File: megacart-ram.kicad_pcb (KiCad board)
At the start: 2 copper layers, 14 parts, among them J1 Conn_02x08_Counter_Clockwise, U1 AS6C4008-55PCN, U10 7432, U11 7432, U12 74LS138, U2 74HC273, U3 74HC74, U4 7421, U5 7421, U6 7402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

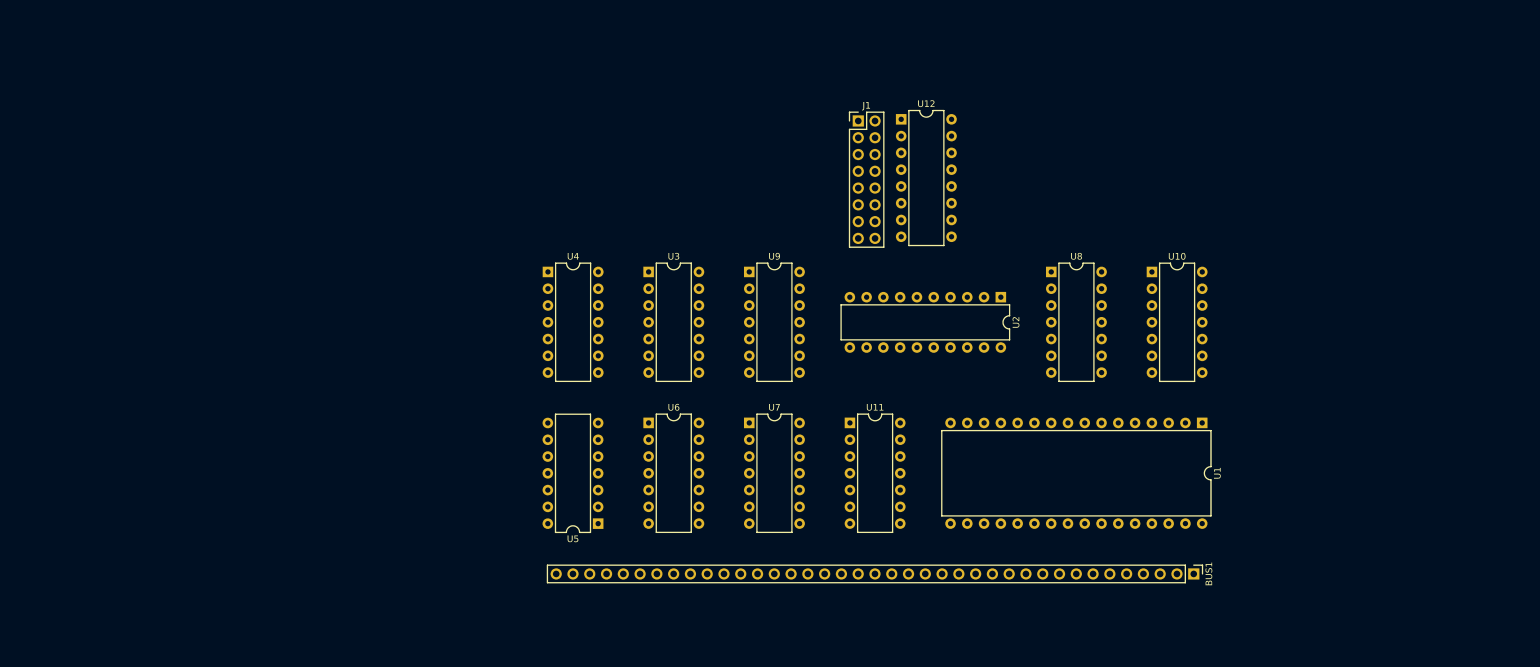
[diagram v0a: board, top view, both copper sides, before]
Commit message: Add decoupling caps and update PCB with RC2014 template.
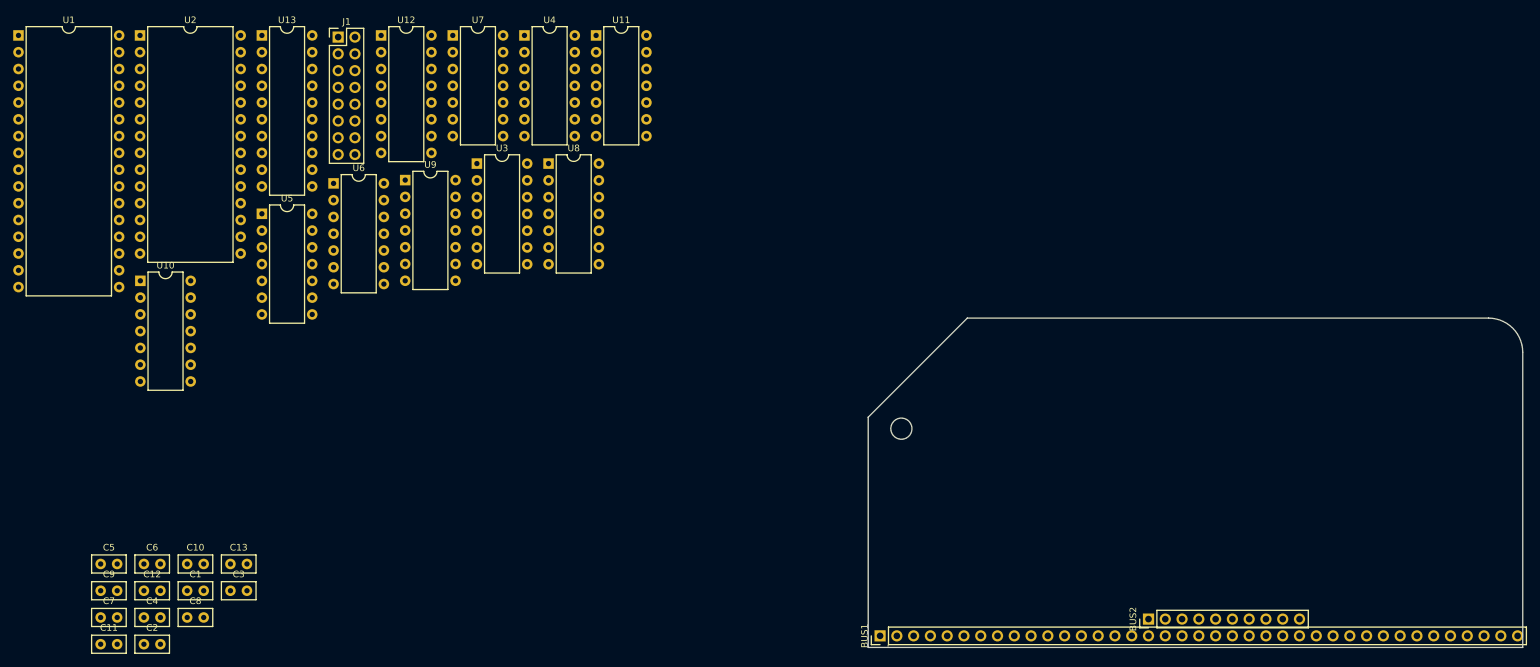
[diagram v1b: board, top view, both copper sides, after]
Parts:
- added ?: , Mounting_Holes:MountingHole_3.2mm_M3, F.Cu at (158.9, 120.2)
- added BUS2: Conn_01x10, Connector_PinHeader_2.54mm:PinHeader_1x10_P2.54mm_Vertical, F.Cu at (196.3, 149.1)
- added C1: C, Capacitor_THT:C_Disc_D5.0mm_W2.5mm_P2.50mm, F.Cu at (50.8, 144.8)
- added C10: C, Capacitor_THT:C_Disc_D5.0mm_W2.5mm_P2.50mm, F.Cu at (50.8, 140.7)
- added C11: C, Capacitor_THT:C_Disc_D5.0mm_W2.5mm_P2.50mm, F.Cu at (37.7, 152.9)
- added C12: C, Capacitor_THT:C_Disc_D5.0mm_W2.5mm_P2.50mm, F.Cu at (44.2, 144.8)
- added C13: C, Capacitor_THT:C_Disc_D5.0mm_W2.5mm_P2.50mm, F.Cu at (57.4, 140.7)
- added C2: C, Capacitor_THT:C_Disc_D5.0mm_W2.5mm_P2.50mm, F.Cu at (44.2, 152.9)
- added C3: C, Capacitor_THT:C_Disc_D5.0mm_W2.5mm_P2.50mm, F.Cu at (57.4, 144.8)
- added C4: C, Capacitor_THT:C_Disc_D5.0mm_W2.5mm_P2.50mm, F.Cu at (44.2, 148.8)
- added C5: C, Capacitor_THT:C_Disc_D5.0mm_W2.5mm_P2.50mm, F.Cu at (37.7, 140.7)
- added C6: C, Capacitor_THT:C_Disc_D5.0mm_W2.5mm_P2.50mm, F.Cu at (44.2, 140.7)
- added C7: C, Capacitor_THT:C_Disc_D5.0mm_W2.5mm_P2.50mm, F.Cu at (37.7, 148.8)
- added C8: C, Capacitor_THT:C_Disc_D5.0mm_W2.5mm_P2.50mm, F.Cu at (50.8, 148.8)
- added C9: C, Capacitor_THT:C_Disc_D5.0mm_W2.5mm_P2.50mm, F.Cu at (37.7, 144.8)
- added U13: 74HC273, Package_DIP:DIP-20_W7.62mm, F.Cu at (62.1, 60.7)
- U2: value 74HC273 -> HM62256BLP; footprint Package_DIP:DIP-20_W7.62mm -> Package_DIP:DIP-28_W15.24mm
- moved U1 188.6 mm to (25.3, 60.7), turned to 0 degrees
- moved U10 153.2 mm to (43.7, 97.9)
- moved U2 136.2 mm to (43.7, 60.7), turned to 0 degrees
- moved J1 79.8 mm to (73.7, 61.0)
- moved U12 79.8 mm to (80.2, 60.7)
- moved U8 77.9 mm to (105.5, 80.1)
- moved U7 73.9 mm to (91.0, 60.7)
- moved U11 70.1 mm to (112.7, 60.7)
- moved U5 69.2 mm to (62.1, 87.7), turned to 0 degrees
- moved U6 59.9 mm to (73.0, 83.1)
- moved U9 53.9 mm to (83.8, 82.6)
- moved BUS1 48.4 mm to (155.7, 151.6), turned to 90 degrees
- moved U4 36.0 mm to (101.9, 60.7)
- moved U3 30.7 mm to (94.7, 80.1)
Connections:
- U10 pad 1: Net-(U6-Pad11) -> Net-(U10-Pad1)
- U10 pad 10: Net-(U8-Pad8) -> Net-(U10-Pad10)
- U10 pad 12: Net-(U6-Pad11) -> Net-(U10-Pad12)
- U10 pad 13: Net-(U8-Pad11) -> Net-(U10-Pad10)
- U10 pad 14: Vcc -> (no net)
- U10 pad 2: Net-(U8-Pad3) -> Net-(U10-Pad10)
- U10 pad 4: Net-(U6-Pad11) -> Net-(U10-Pad4)
- U10 pad 5: Net-(U8-Pad6) -> Net-(U10-Pad10)
- U10 pad 7: Gnd -> (no net)
- U10 pad 9: Net-(U6-Pad11) -> Net-(U10-Pad9)
- U11 pad 1: Net-(U6-Pad11) -> Net-(U11-Pad1)
- U11 pad 10: (no net) -> Net-(U11-Pad10)
- U11 pad 14: Vcc -> (no net)
- U11 pad 2: Net-(U9-Pad3) -> Net-(U10-Pad10)
- U11 pad 6: unconnected-(U11-Pad6) -> ~{MWR}
- U11 pad 7: Gnd -> (no net)
- U11 pad 8: (no net) -> Net-(U11-Pad8)
- U11 pad 9: (no net) -> A15
- U2 pad 1: ~{RESET} -> A14
- U2 pad 10: GND -> A0
- U2 pad 11: Net-(U2-Pad11) -> D0
- U2 pad 12: Net-(U2-Pad12) -> D1
- U2 pad 13: A4 -> D2
- U2 pad 14: unconnected-(U2-Pad14) -> GND
- U2 pad 15: unconnected-(U2-Pad15) -> D3
- U2 pad 16: unconnected-(U2-Pad16) -> D4
- U2 pad 17: unconnected-(U2-Pad17) -> D5
- U2 pad 18: unconnected-(U2-Pad18) -> D6
- U2 pad 19: unconnected-(U2-Pad19) -> D7
- U2 pad 2: Net-(U2-Pad2) -> A12
- U2 pad 20: VCC -> Net-(U11-Pad8)
- U2 pad 3: A0 -> A7
- U2 pad 4: A1 -> A6
- U2 pad 5: Net-(U2-Pad5) -> A5
- U2 pad 6: Net-(U2-Pad6) -> A4
- U2 pad 7: A2 -> A3
- U2 pad 8: A3 -> A2
- U2 pad 9: Net-(U2-Pad9) -> A1
- U3 pad 10: unconnected-(U3-Pad10) -> VCC
- U3 pad 4: unconnected-(U3-Pad4) -> VCC
- U4 pad 14: Vcc -> (no net)
- U4 pad 7: Gnd -> (no net)
- U5 pad 14: Vcc -> (no net)
- U5 pad 7: Gnd -> (no net)
- U5 pad 8: Net-(U2-Pad11) -> Net-(U13-Pad11)
- U6 pad 11: Net-(U6-Pad11) -> Net-(U10-Pad10)
- U6 pad 4: Net-(U6-Pad11) -> Net-(U10-Pad10)
- U7 pad 12: (no net) -> Net-(U11-Pad10)
- U7 pad 13: (no net) -> PAGE
- U8 pad 1: Net-(U7-Pad8) -> Net-(U13-Pad2)
- U8 pad 10: Net-(U2-Pad6) -> Net-(U7-Pad8)
- U8 pad 11: Net-(U8-Pad11) -> Net-(U10-Pad12)
- U8 pad 12: Net-(U7-Pad8) -> Net-(U13-Pad9)
- U8 pad 13: Net-(U2-Pad9) -> Net-(U7-Pad8)
- U8 pad 14: Vcc -> (no net)
- U8 pad 2: Net-(U2-Pad2) -> Net-(U7-Pad8)
- U8 pad 3: Net-(U8-Pad3) -> Net-(U10-Pad1)
- U8 pad 4: Net-(U7-Pad8) -> Net-(U13-Pad5)
- U8 pad 5: Net-(U2-Pad5) -> Net-(U7-Pad8)
- U8 pad 6: Net-(U8-Pad6) -> Net-(U10-Pad4)
- U8 pad 7: Gnd -> (no net)
- U8 pad 8: Net-(U8-Pad8) -> Net-(U10-Pad9)
- U8 pad 9: Net-(U7-Pad8) -> Net-(U13-Pad6)
- U9 pad 1: Net-(U7-Pad8) -> Net-(U13-Pad12)
- U9 pad 14: Vcc -> (no net)
- U9 pad 2: Net-(U2-Pad12) -> Net-(U7-Pad8)
- U9 pad 3: Net-(U9-Pad3) -> Net-(U11-Pad1)
- U9 pad 7: Gnd -> (no net)
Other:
- board outline added: 99.1 x 49.9 mm
- rule pad_to_mask_clearance: 0 -> 0.2

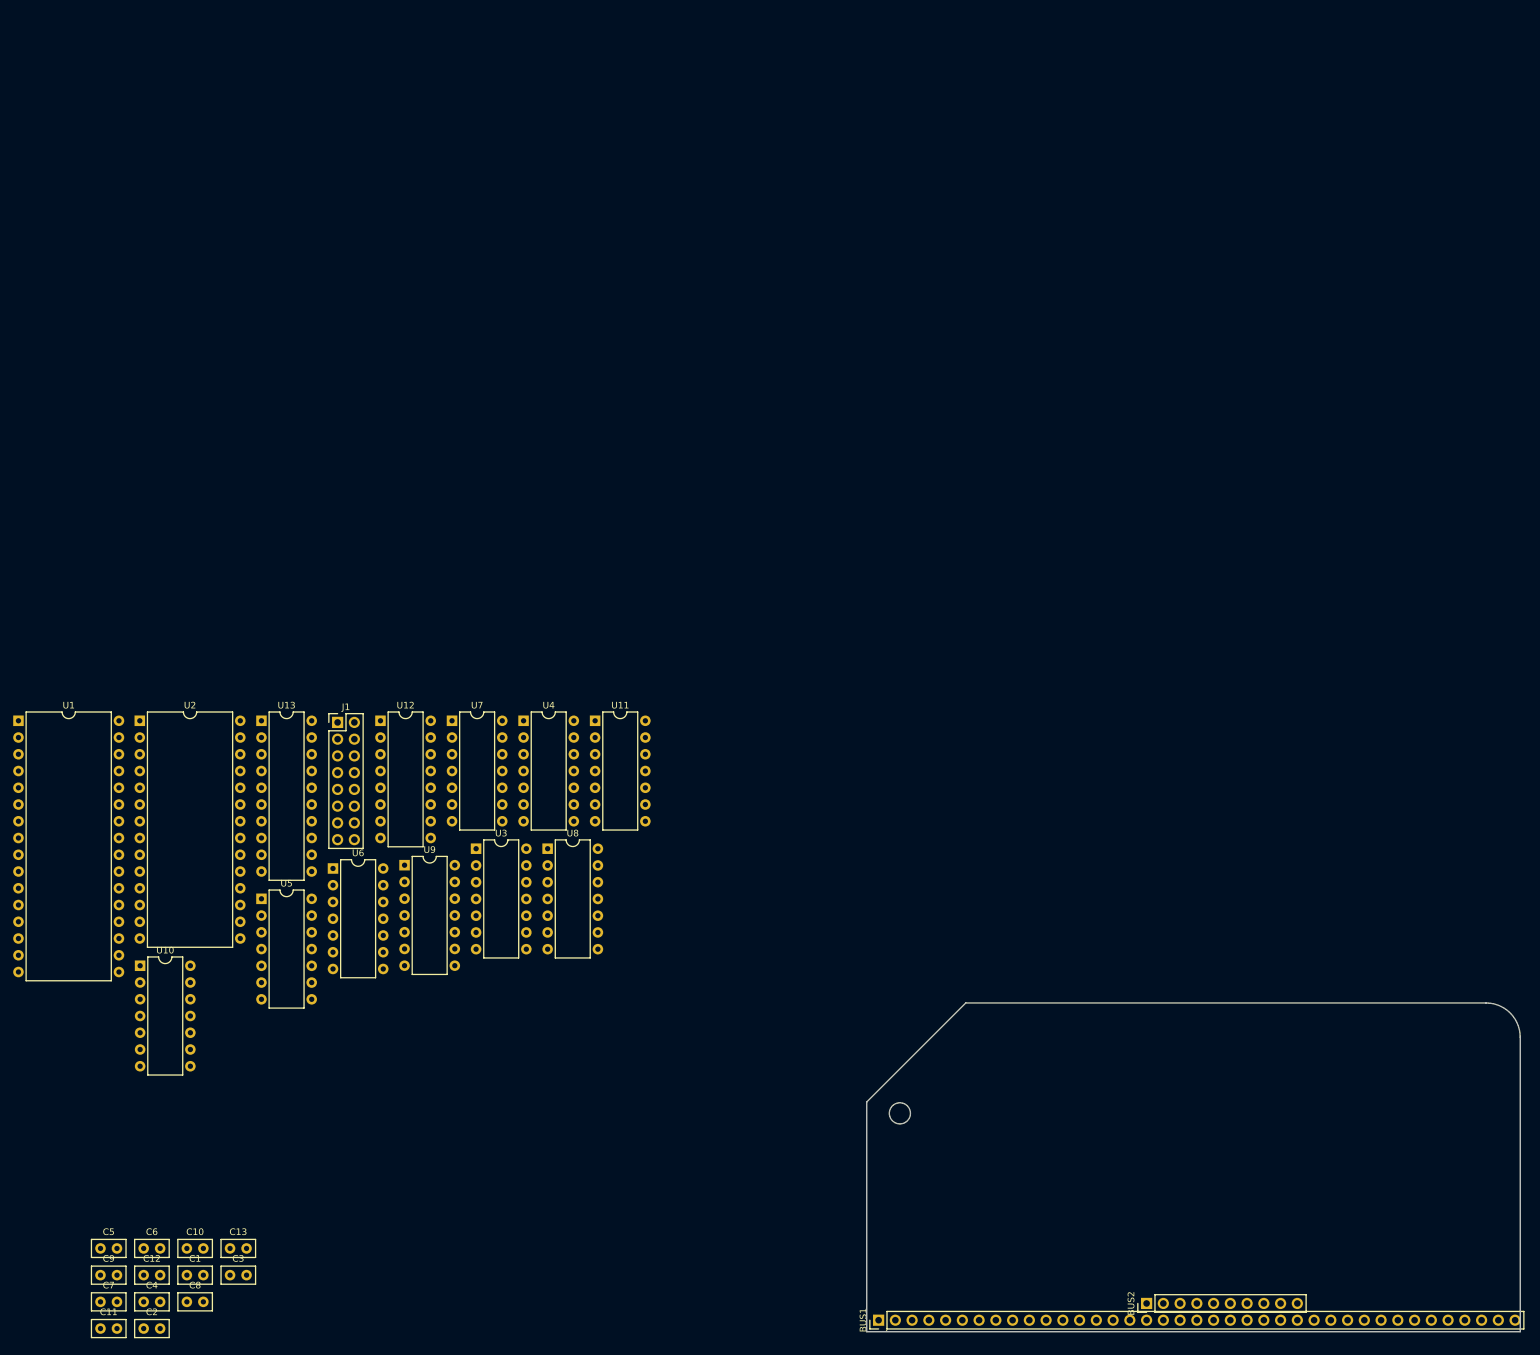
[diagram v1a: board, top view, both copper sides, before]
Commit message: Add explicit power units for 7400 ICs.
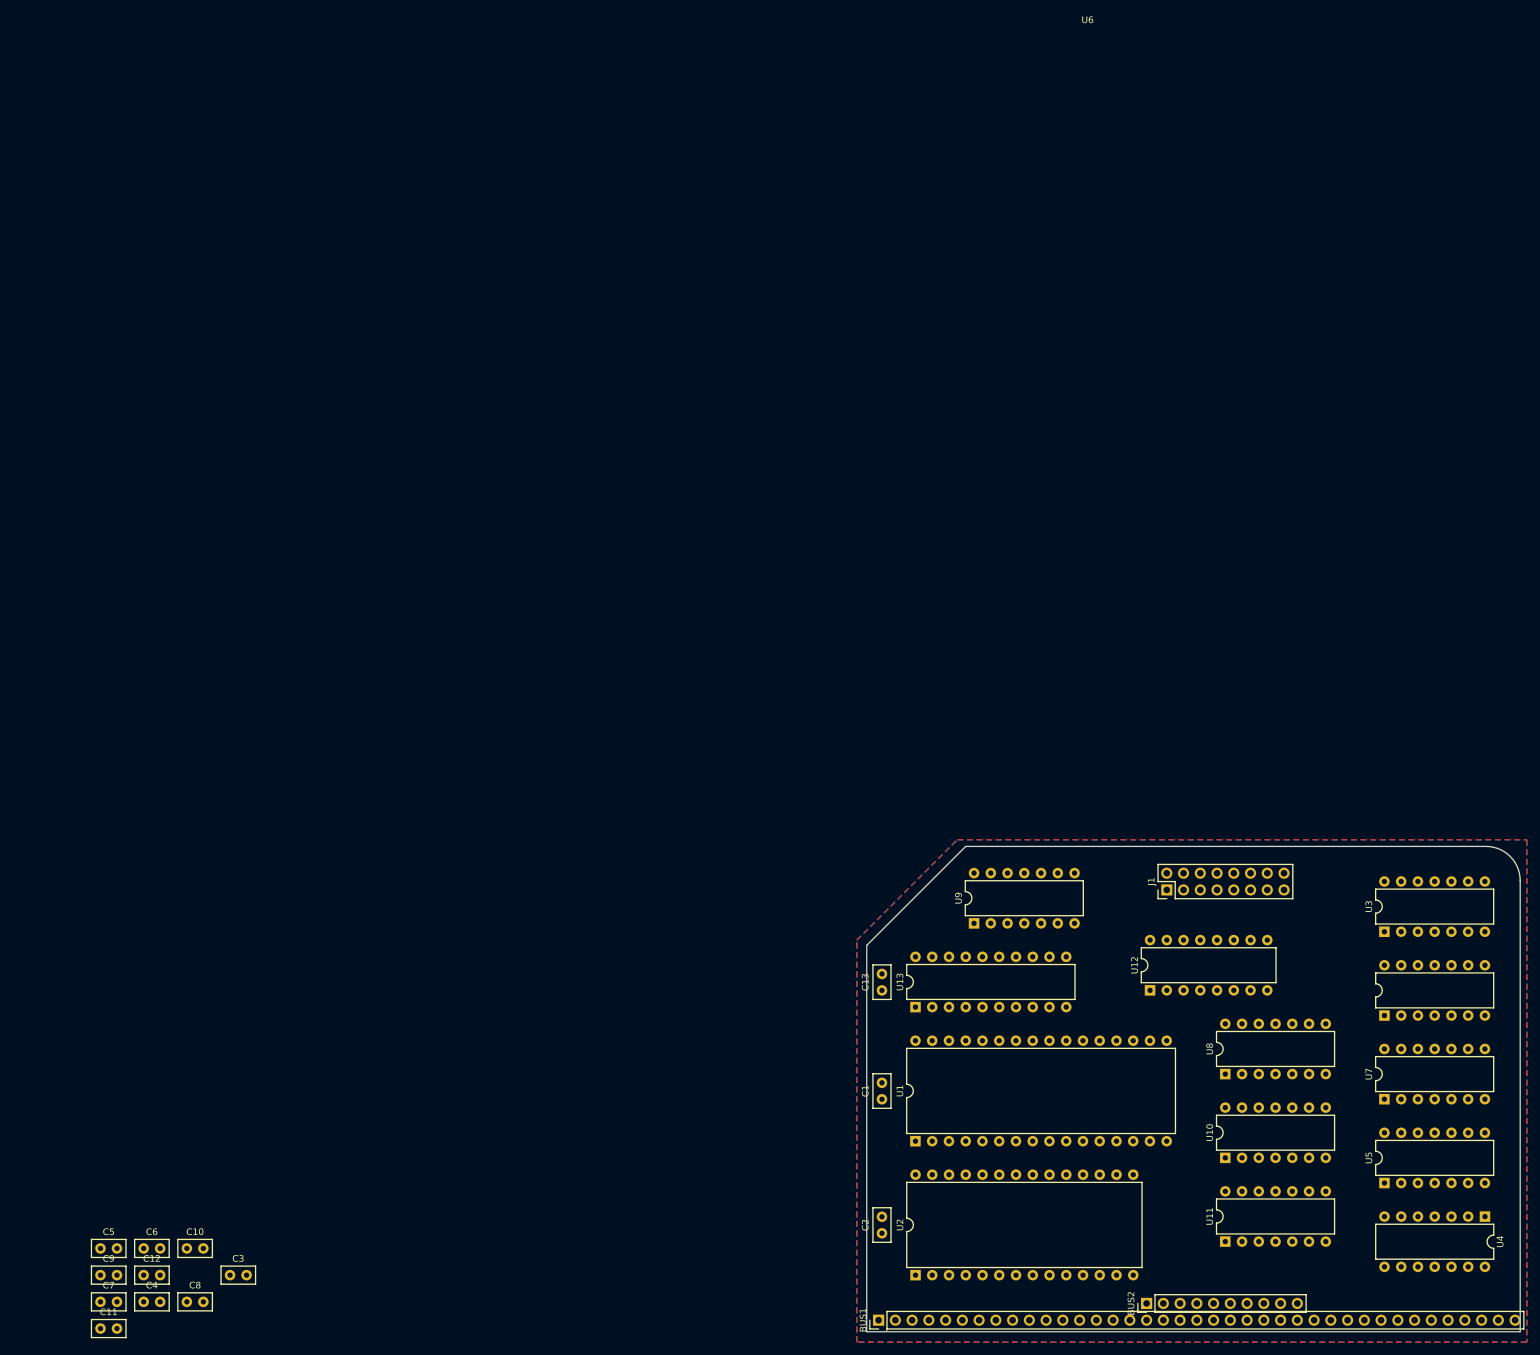
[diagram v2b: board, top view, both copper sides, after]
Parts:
- removed ?: , Mounting_Holes:MountingHole_3.2mm_M3
- moved U5 175.7 mm to (232.4, 130.8), turned to 90 degrees
- moved U10 167.1 mm to (208.3, 127.0), turned to 90 degrees
- moved U4 164.0 mm to (247.7, 135.9), turned to -90 degrees
- moved U6 161.0 mm to (232.4, 105.4), turned to 90 degrees
- moved U7 152.6 mm to (232.4, 118.1), turned to 90 degrees
- moved U1 150.2 mm to (161.3, 124.5), turned to 90 degrees
- moved U2 144.6 mm to (161.3, 144.8), turned to 90 degrees
- moved U3 138.3 mm to (232.4, 92.7), turned to 90 degrees
- moved J1 128.3 mm to (199.4, 86.4), turned to 90 degrees
- moved U11 124.0 mm to (208.3, 139.7), turned to 90 degrees
- moved U12 123.7 mm to (196.9, 101.6), turned to 90 degrees
- moved C2 112.9 mm to (156.2, 138.4), turned to 90 degrees
- moved C1 108.7 mm to (156.2, 118.1), turned to 90 degrees
- moved U8 108.3 mm to (208.3, 114.3), turned to 90 degrees
- moved U13 108.3 mm to (161.3, 104.1), turned to 90 degrees
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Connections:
- U10 pad 14: (no net) -> VCC
- U10 pad 7: (no net) -> GND
- U11 pad 14: (no net) -> VCC
- U11 pad 7: (no net) -> GND
- U4 pad 14: (no net) -> VCC
- U4 pad 7: (no net) -> GND
- U5 pad 14: (no net) -> VCC
- U5 pad 7: (no net) -> GND
- U6 pad 14: (no net) -> VCC
- U6 pad 7: (no net) -> GND
- U7 pad 14: (no net) -> VCC
- U7 pad 7: (no net) -> GND
- U8 pad 14: (no net) -> VCC
- U8 pad 7: (no net) -> GND
- U9 pad 14: (no net) -> VCC
- U9 pad 7: (no net) -> GND
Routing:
- added copper zone on F.Cu, net GND
- added copper zone on B.Cu, net VCC
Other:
- board size 99.1 x 49.9 mm -> 99.1 x 73.6 mm

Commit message: First pass at routing PCB.
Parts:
- removed C4, C5, C8: C, Capacitor_THT:C_Disc_D5.0mm_W2.5mm_P2.50mm
- moved C7 214.1 mm to (250.2, 122.4), turned to 180 degrees
- moved C11 204.8 mm to (230.1, 82.8), turned to -90 degrees
- moved C6 198.9 mm to (238.0, 95.8), turned to -90 degrees
- moved C12 186.9 mm to (231.1, 141.8), turned to -90 degrees
- moved C9 184.1 mm to (220.5, 122.4), turned to 180 degrees
- moved C3 175.7 mm to (231.7, 122.4)
- moved C10 122.8 mm to (163.8, 92.7), turned to 180 degrees
- moved U4 84.3 mm to (182.0, 83.0), turned to 0 degrees
- moved J1 64.4 mm to (247.6, 129.0), turned to 0 degrees
- moved C13 60.3 mm to (207.8, 132.8), turned to 0 degrees
- moved U10 58.3 mm to (170.0, 83.0), turned to 0 degrees
- moved U11 57.5 mm to (218.0, 83.0), turned to 0 degrees
- moved U5 54.6 mm to (206.0, 83.0), turned to 0 degrees
- moved U9 49.2 mm to (218.0, 103.0), turned to 0 degrees
- moved U12 45.5 mm to (234.9, 126.5), turned to 0 degrees
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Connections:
- J1 pad 11: Net-(J1-Pad10) -> Net-(J1-Pad11)
- J1 pad 13: Net-(J1-Pad10) -> Net-(J1-Pad13)
- J1 pad 15: Net-(J1-Pad10) -> Net-(J1-Pad15)
- J1 pad 2: Net-(J1-Pad2) -> Net-(J1-Pad10)
- J1 pad 4: Net-(J1-Pad4) -> Net-(J1-Pad10)
- J1 pad 6: Net-(J1-Pad6) -> Net-(J1-Pad10)
- J1 pad 8: Net-(J1-Pad8) -> Net-(J1-Pad10)
- J1 pad 9: Net-(J1-Pad10) -> Net-(J1-Pad9)
- U11 pad 11: (no net) -> unconnected-(U11-Pad11)
- U11 pad 12: (no net) -> GND
- U11 pad 13: (no net) -> GND
- U12 pad 10: Net-(J1-Pad6) -> Net-(J1-Pad11)
- U12 pad 11: Net-(J1-Pad5) -> Net-(J1-Pad9)
- U12 pad 12: Net-(J1-Pad4) -> Net-(J1-Pad7)
- U12 pad 13: Net-(J1-Pad3) -> Net-(J1-Pad5)
- U12 pad 14: Net-(J1-Pad2) -> Net-(J1-Pad3)
- U12 pad 7: Net-(J1-Pad8) -> Net-(J1-Pad15)
- U12 pad 9: Net-(J1-Pad7) -> Net-(J1-Pad13)
- U3 pad 14: (no net) -> VCC
- U3 pad 7: (no net) -> GND
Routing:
- net VCC: track 0.00 -> 195.6 mm, vias 0 -> 6
- net A15: track 0.00 -> 179.6 mm, vias 0 -> 2
- net A5: track 0.00 -> 145.9 mm, vias 0 -> 1
- net A6: track 0.00 -> 145.5 mm, vias 0 -> 1
- net A7: track 0.00 -> 144.8 mm, vias 0 -> 3
- net A14: track 0.00 -> 142.4 mm, vias 0 -> 1
- net GND: track 0.00 -> 136.5 mm, vias 0 -> 2
- net D1: track 0.00 -> 119.3 mm
- net D0: track 0.00 -> 118.0 mm, vias 0 -> 1
- net A4: track 0.00 -> 110.9 mm, vias 0 -> 2
- net A13: track 0.00 -> 108.1 mm
- net A3: track 0.00 -> 107.6 mm, vias 0 -> 2
- net CLK: track 0.00 -> 106.8 mm, vias 0 -> 2
- net Net-(U10-Pad10): track 0.00 -> 104.1 mm, vias 0 -> 1
- net Net-(U7-Pad8): track 0.00 -> 102.8 mm, vias 0 -> 2
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
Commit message: Routing optimizations.
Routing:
- net VCC: track 195.6 -> 169.1 mm, vias 6 -> 5
- net Net-(U4-Pad8): track 35.1 -> 34.5 mm
- net BSH: track 53.8 -> 53.7 mm, vias 1 -> 2
- net Net-(U13-Pad12): vias 3 -> 2
- net A0: vias 2 -> 1

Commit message: Finalize PCB design.
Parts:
- added C4: C, Capacitor_THT:C_Disc_D5.0mm_W2.5mm_P2.50mm, F.Cu at (157.8, 97.3)
- added C5: C, Capacitor_THT:C_Disc_D5.0mm_W2.5mm_P2.50mm, F.Cu at (234.6, 82.8)
- added C8: C, Capacitor_THT:C_Disc_D5.0mm_W2.5mm_P2.50mm, F.Cu at (157.7, 101.7)
- U10, U11: value 7432 -> 74HCT32
- U12: value 74LS138 -> 74HCT138
- U13: value 74HC273 -> 74HCT273
- U2: value HM62256BLP -> AS6C62256-55PCN
- U3: value 74HC74 -> 74HCT74
- U4, U5: value 7421 -> 74HCT21
- U6: value 7402 -> 74HCT02
- U7: value 74HC04 -> 74HCT04
- U8, U9: value 7408 -> 74HCT08
- moved C10 2.54 mm to (163.8, 90.2), turned to -90 degrees
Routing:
- net GND: track 136.5 -> 133.4 mm
- net VCC: track 169.1 -> 166.5 mm
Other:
- board text added: "RC2014 ColecoVision MegaCart 32KB/512KB RAM Module by Aaron Mavrinac"
